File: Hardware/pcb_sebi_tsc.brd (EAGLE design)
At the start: 46 x 35 mm, 105 parts, among them IC1 BQ25180YBGR, IC2 DRV2605YZFR, IC3 BMA421, IC9 RT6160AWSC, J1 503480-2400, J2 TC2030-IDC, J4 KH-TYPE-C-16P, Q3 SI1308EDL-T1-GE3, U1 NRF52840_QF, U3 MAX17048G+T10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

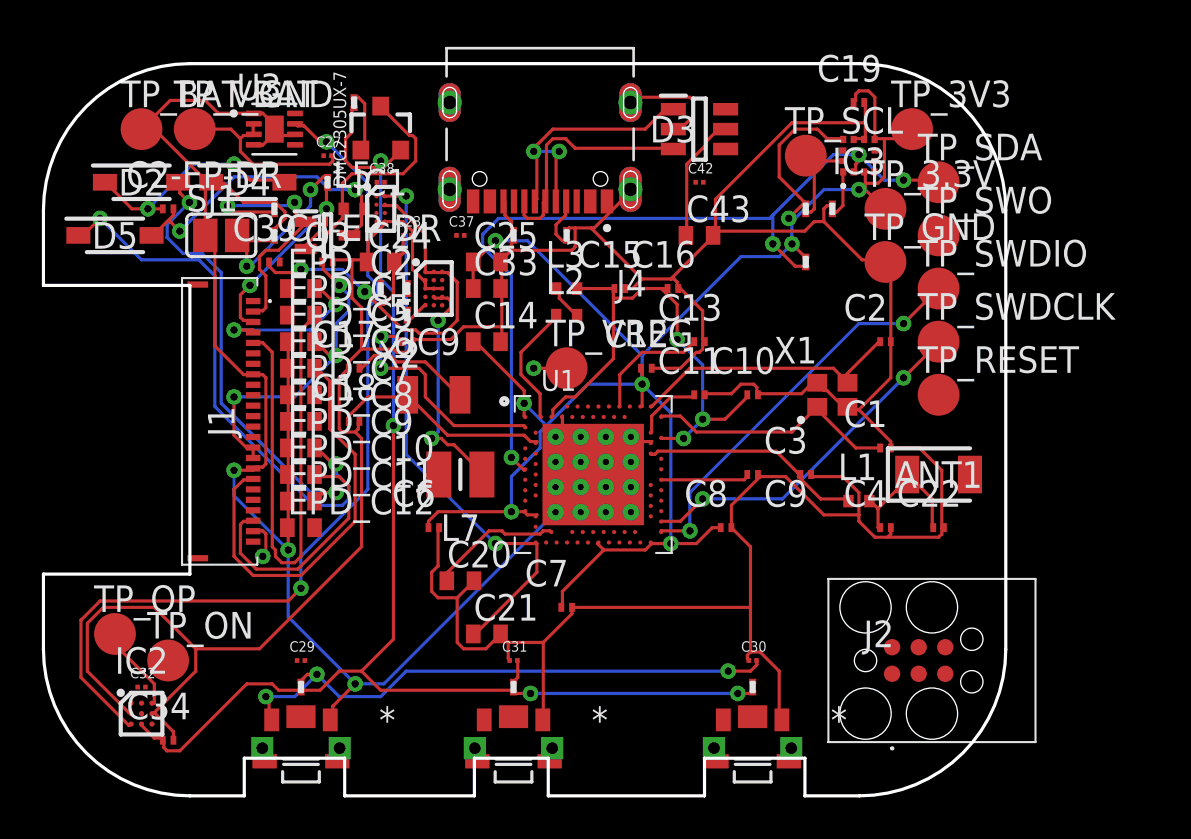
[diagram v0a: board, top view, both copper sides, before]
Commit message: manual route
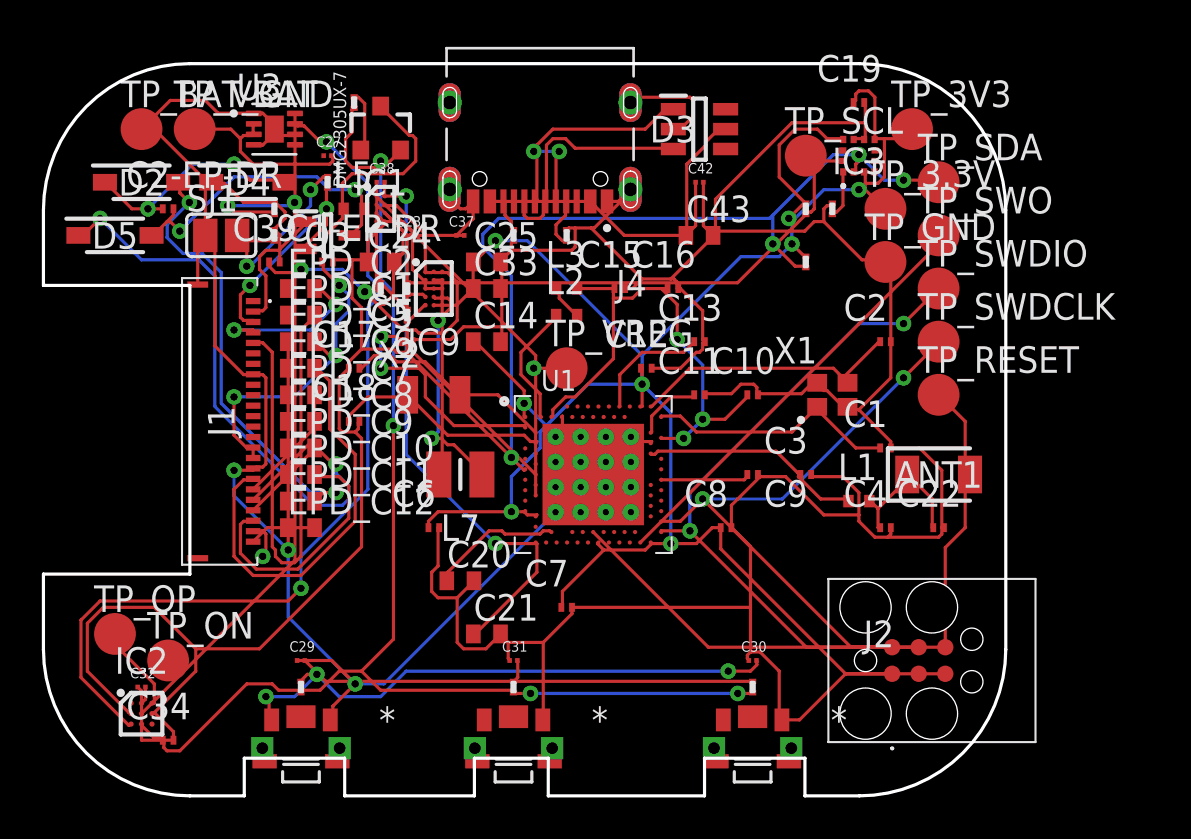
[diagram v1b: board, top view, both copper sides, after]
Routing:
- net SCL/2.4C: track 4.89 -> 41.3 mm
- net RESET: track 0.00 -> 32.1 mm
- net SDA/1.4C: track 0.00 -> 31.7 mm
- net GND: track 282.8 -> 312.9 mm
- net N$36: track 0.00 -> 21.8 mm
- net SWO: track 0.00 -> 20.6 mm
- net PMIC_INT: track 0.00 -> 17.5 mm
- net SDA/2.4C: track 40.5 -> 54.9 mm
- net 3V3/2.4A: track 90.4 -> 104.3 mm
- net SWDCLK: track 16.9 -> 30.1 mm
- net VBUS/1.5D: track 6.06 -> 18.8 mm
- net SWDIO: track 19.2 -> 31.2 mm
- net LX1: track 0.00 -> 9.29 mm
- net N$29: track 0.00 -> 5.74 mm
- net N$30: track 0.00 -> 4.97 mm
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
